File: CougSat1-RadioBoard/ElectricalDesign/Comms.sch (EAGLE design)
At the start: 409 parts, among them J1 700mm Antenna, J2 CougSat Card, J3 230mm Antenna, J4 SWD, Q1 DMN53D0LDW, Q2 DMN53D0LDW, Q3 DMN53D0LDW, Q4 CSD25402Q3A, Q5 CSD25402Q3A, U1 AD8515, U10 AD8515, U11 AD8515, U12 TXS0102DQM, U13 ADF4360, U14 MAAM-011229, U15 INA199C2, U16 AD8515, U17 AD8515, U18 LP5907MFX-3.1, U19 HMC545A, U2 AD8515, U20 INA199C1, U21 TPS61236, U22 AD8345, U23 AD9761, U24 TXS0102DQM, U25 TXS0102DQM, U26 TXS0102DQM, U27 MMZ09332B, U28 AD8515, U29 ADF4360, U3 AD7291, U30 TXS0102DQM, U31 INA199C2, U32 TXS0102DQM, U33 LP5907MFX-3.1, U34 MAAM-011229, U35 TXS0102DQM, U36 TXS0102DQM, U37 AD9761, U38 AD8346, U39 TXS0102DQM, U4 AD7291, U40 STM32L496VGT, U41 HMC452QS16G, U42 TXS0102DQM, U43 INA199C2, U44 ADF4360, U45 LP5907MFX-3.1, U46 IS25LP016D, U47 IS25LP016D, U48 GRF2133, U49 INA199C1, U5 MAAM-011229, U6 AD8348, U7 AD7291, U8 MAAM-011229, U9 TXS0102DQM, Y1 19.68MHz ±2.5ppm, Y2 19.68MHz ±2.5ppm, Y3 8MHz ±10ppm, Y4 32.768kHz ±10ppm, Y5 19.68MHz ±2.5ppm

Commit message: Removed 230mm circuits
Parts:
- removed C140, C143, C176: 1nF 1%, CougsInSpace-Capacitors:CAP-H-1NF-B-1608
- removed C141, C170, C172, C173, C174, C185: 1µF 10%, CougsInSpace-Capacitors:CAP-V-1UF-B-1608
- removed C142: 560pF 1%, CougsInSpace-Capacitors:CAP-V-560PF-1608
- removed C144: 100pF 1%, CougsInSpace-Capacitors:CAP-H-100PF-1608
- removed C145: 2pF ±0.1pF, CougsInSpace-Capacitors:CAP-V-2PF-1608
- removed C146, C147, C150, C156, C157, C158, C159, C160, C161, C163, C165, C166, C175, C178, C179, C180, C183, C184: 100nF 10%, CougsInSpace-Capacitors:CAP-V-100NF-1608
- removed C148, C171: 10nF 10%, CougsInSpace-Capacitors:CAP-V-10NF-1608
- removed C149, C168: 100pF 1%, CougsInSpace-Capacitors:CAP-V-100PF-1608
- removed C151, C155: 8pF ±0.25, CougsInSpace-Capacitors:CAP-V-8PF-1608
- removed C152: 56pF 2%, CougsInSpace-Capacitors:CAP-V-56PF-1608
- removed C153: 270pF 1%, CougsInSpace-Capacitors:CAP-V-270PF-1608
- removed C154: 10pF 5%, CougsInSpace-Capacitors:CAP-V-10PF-1608
- removed C162, C167: 15pF 1%, CougsInSpace-Capacitors:CAP-V-15PF-1608
- removed C164: 0.8pF ±0.1pF, CougsInSpace-Capacitors:CAP-H-0.8PF-1608
- removed C169: 4.7pF ±0.1, CougsInSpace-Capacitors:CAP-V-4.7PF-1608
- removed C177: 10pF 5%, CougsInSpace-Capacitors:CAP-H-10PF-1608
- removed C181, C182: 33pF 5%, CougsInSpace-Capacitors:CAP-H-33PF-1608
- removed FB8: 1.5kΩ @ 100MHz, CougsInSpace-Coils:CHOKE-V-1.5K-1608
- removed H5, H6, H7: M2, CougsInSpace-Hardware:MOUNTING_HOLE-2.2
- removed J4: SWD, CougsInSpace-Connectors:SWDSMD-6-R
- removed L13, L20: 22nH 2%, CougsInSpace-Coils:INDUCTOR-V-22NH-1608
- removed L14, L15, L16: 1.6nH 5%, CougsInSpace-Coils:INDUCTOR-V-1.6NH-1608
- removed L17: 22nH 2%, CougsInSpace-Coils:INDUCTOR-H-22NH-1608
- removed L18: 33nH 2%, CougsInSpace-Coils:INDUCTOR-V-33NH-1608
- removed L19: 18nH 2%, CougsInSpace-Coils:INDUCTOR-V-18NH-1608
- removed Q5: CSD25402Q3A, CougsInSpace-DiscreteSemi:MOSFET-P-SON-3333
- removed R75, R82, R89: 1kΩ 0.1%, CougsInSpace-Resistors:RES-V-1K-1608
- removed R76, R80: 49.9Ω 0.1%, CougsInSpace-Resistors:RES-V-49.9-1608
- removed R77, R79: 1.33kΩ 0.1%, CougsInSpace-Resistors:RES-V-1.33K-1608
- removed R78: 1.74kΩ 0.1%, CougsInSpace-Resistors:RES-V-1.74K-1608
- removed R81: 5.6Ω 1%, CougsInSpace-Resistors:RES-V-5.6R-1608
- removed R83: 102kΩ 0.1%, CougsInSpace-Resistors:RES-V-102K-1608
- removed R84: 0Ω <20mΩ, CougsInSpace-Resistors:RES-V-0-1608
- removed R85, R93: 50mΩ 1%, CougsInSpace-Resistors:RES-V-0.05R-1608
- removed R86, R92, R94, R95: 10kΩ 0.1%, CougsInSpace-Resistors:RES-V-10K-1608
- removed R87, R91: 4.7kΩ 0.1%, CougsInSpace-Resistors:RES-V-4.7K-1608
- removed R88: 75Ω 0.1%, CougsInSpace-Resistors:RES-V-75R-1608
- removed R90: 0Ω <20mΩ, CougsInSpace-Resistors:RES-H-0-1608
- removed U40: STM32L496VGT, CougsInSpace-IC-µController:STM32-100P-L496VGT
- removed U41: HMC452QS16G, CougsInSpace-RF:AMP-BIAS-HMC452QS16G
- removed U42: TXS0102DQM, CougsInSpace-IC-Comms:LEVEL_SHIFTER-2BIT-XSON-8
- removed U43: INA199C2, CougsInSpace-IC-Amplifiers:INA199C2
- removed U44: ADF4360, CougsInSpace-RF:ADF4360
- removed U45: LP5907MFX-3.1, CougsInSpace-IC-Power:LDO-3.1-SOT23-5
- removed U46, U47: IS25LP016D, CougsInSpace-IC-Memory:FLASH-(Q)SPI-2MB-SO8
- removed U48: GRF2133, CougsInSpace-RF:GRF2133
- removed U49: INA199C1, CougsInSpace-IC-Amplifiers:INA199C1
- removed Y5: 19.68MHz ±2.5ppm, CougsInSpace-Clocks:OSCILLATOR-19.68M-SMD-3225
- C112: value 100nF 10% -> 2.4pF ±0.1pF; device CougsInSpace-Capacitors:CAP-V-100NF-1608 -> CougsInSpace-Capacitors:CAP-H-2.4PF-1608
- C113: value 2.4pF ±0.1pF -> 100nF 10%; device CougsInSpace-Capacitors:CAP-H-2.4PF-1608 -> CougsInSpace-Capacitors:CAP-V-100NF-1608
- C114: value 100nF 10% -> 47pF 5%; device CougsInSpace-Capacitors:CAP-V-100NF-1608 -> CougsInSpace-Capacitors:CAP-V-47PF-1608
- C115: value 47pF 5% -> 100pF 1%; device CougsInSpace-Capacitors:CAP-V-47PF-1608 -> CougsInSpace-Capacitors:CAP-V-100PF-1608
- C116: value 100pF 1% -> 1µF 10%; device CougsInSpace-Capacitors:CAP-V-100PF-1608 -> CougsInSpace-Capacitors:CAP-V-1UF-B-1608
- C117: value 1µF 10% -> 1nF 1%; device CougsInSpace-Capacitors:CAP-V-1UF-B-1608 -> CougsInSpace-Capacitors:CAP-V-1NF-B-1608
- C118, C128: value 1nF 1% -> 100nF 10%; device CougsInSpace-Capacitors:CAP-V-1NF-B-1608 -> CougsInSpace-Capacitors:CAP-V-100NF-1608
- C119: value 100nF 10% -> 1µF 10%; device CougsInSpace-Capacitors:CAP-V-100NF-1608 -> CougsInSpace-Capacitors:CAP-V-1UF-B-1608
- C120: value 1µF 10% -> 1nF 1%; device CougsInSpace-Capacitors:CAP-V-1UF-B-1608 -> CougsInSpace-Capacitors:CAP-H-1NF-B-1608
- C121, C124: value 1nF 1% -> 1µF 10%; device CougsInSpace-Capacitors:CAP-H-1NF-B-1608 -> CougsInSpace-Capacitors:CAP-V-1UF-B-1608
- C122: value 1µF 10% -> 10nF 10%; device CougsInSpace-Capacitors:CAP-V-1UF-B-1608 -> CougsInSpace-Capacitors:CAP-V-10NF-1608
- C123: value 10nF 10% -> 1nF 1%; device CougsInSpace-Capacitors:CAP-V-10NF-1608 -> CougsInSpace-Capacitors:CAP-H-1NF-B-1608
- C125: value 1µF 10% -> 100nF 10%; device CougsInSpace-Capacitors:CAP-V-1UF-B-1608 -> CougsInSpace-Capacitors:CAP-V-100NF-1608
- C127: value 100nF 10% -> 1nF 1%; device CougsInSpace-Capacitors:CAP-V-100NF-1608 -> CougsInSpace-Capacitors:CAP-V-1NF-B-1608
- C130: value 560pF 1% -> 100nF 10%; device CougsInSpace-Capacitors:CAP-V-560PF-1608 -> CougsInSpace-Capacitors:CAP-V-100NF-1608
- C131: value 100nF 10% -> 8pF ±0.25; device CougsInSpace-Capacitors:CAP-V-100NF-1608 -> CougsInSpace-Capacitors:CAP-V-8PF-1608
- C132: value 100pF 1% -> 8pF ±0.25; device CougsInSpace-Capacitors:CAP-H-100PF-1608 -> CougsInSpace-Capacitors:CAP-V-8PF-1608
- C134, C136: value 100nF 10% -> 15pF 1%; device CougsInSpace-Capacitors:CAP-V-100NF-1608 -> CougsInSpace-Capacitors:CAP-V-15PF-1608
- C137: value 100pF 1% -> 100nF 10%; device CougsInSpace-Capacitors:CAP-V-100PF-1608 -> CougsInSpace-Capacitors:CAP-V-100NF-1608
- C138: value 10nF 10% -> 100nF 10%; device CougsInSpace-Capacitors:CAP-V-10NF-1608 -> CougsInSpace-Capacitors:CAP-V-100NF-1608
- C139: value 4.7pF ±0.1 -> 100nF 10%; device CougsInSpace-Capacitors:CAP-V-4.7PF-1608 -> CougsInSpace-Capacitors:CAP-V-100NF-1608
- H3: value Can - 230mm -> M2; device CougsInSpace-Hardware:SHIELDING-2641 -> CougsInSpace-Hardware:MOUNTING_HOLE-2.2
- J3: value 230mm Antenna -> SWD; device CougsInSpace-Connectors:COAX-U.FL -> CougsInSpace-Connectors:SWDSMD-6-R
- LOGO1: value SIGNATUREBRADLEY -> Satellite 16mm; device CougsInSpace-Aesthetics:SIGNATUREBRADLEY -> CougsInSpace-Aesthetics:CIS-LOGO-SATELLITE-16MM
- LOGO2: value Satellite 16mm -> SIGNATUREBRADLEY; device CougsInSpace-Aesthetics:CIS-LOGO-SATELLITE-16MM -> CougsInSpace-Aesthetics:SIGNATUREBRADLEY
- R61: value 0Ω <20mΩ -> 2kΩ 0.1%; device CougsInSpace-Resistors:RES-V-0-1608 -> CougsInSpace-Resistors:RES-V-2K-1608
- R62: value 2kΩ 0.1% -> 470Ω 0.5%; device CougsInSpace-Resistors:RES-V-2K-1608 -> CougsInSpace-Resistors:RES-V-470R-1608
- R63: value 470Ω 0.5% -> 1.74kΩ 0.1%; device CougsInSpace-Resistors:RES-V-470R-1608 -> CougsInSpace-Resistors:RES-V-1.74K-1608
- R64: value 1.74kΩ 0.1% -> 50mΩ 1%; device CougsInSpace-Resistors:RES-V-1.74K-1608 -> CougsInSpace-Resistors:RES-V-0.05R-1608
- R65: value 50mΩ 1% -> 10kΩ 0.1%; device CougsInSpace-Resistors:RES-V-0.05R-1608 -> CougsInSpace-Resistors:RES-V-10K-1608
- R66: value 10kΩ 0.1% -> 4.7kΩ 0.1%; device CougsInSpace-Resistors:RES-V-10K-1608 -> CougsInSpace-Resistors:RES-V-4.7K-1608
- R67: value 4.7kΩ 0.1% -> 2kΩ 0.1%; device CougsInSpace-Resistors:RES-V-4.7K-1608 -> CougsInSpace-Resistors:RES-V-2K-1608
- R69: value 2kΩ 0.1% -> 1kΩ 0.1%; device CougsInSpace-Resistors:RES-V-2K-1608 -> CougsInSpace-Resistors:RES-V-1K-1608
- R71: value 1.33kΩ 0.1% -> 1kΩ 0.1%; device CougsInSpace-Resistors:RES-V-1.33K-1608 -> CougsInSpace-Resistors:RES-V-1K-1608
- R72: value 1.74kΩ 0.1% -> 0Ω <20mΩ; device CougsInSpace-Resistors:RES-V-1.74K-1608 -> CougsInSpace-Resistors:RES-H-0-1608
- R73: value 1.33kΩ 0.1% -> 10kΩ 0.1%; device CougsInSpace-Resistors:RES-V-1.33K-1608 -> CougsInSpace-Resistors:RES-V-10K-1608
- R74: value 8.45kΩ 0.1% -> 10kΩ 0.1%; device CougsInSpace-Resistors:RES-V-8.45K-1608 -> CougsInSpace-Resistors:RES-V-10K-1608
- U37: value AD9761 -> STM32L496VGT; device CougsInSpace-IC-Conversion:AD9761 -> CougsInSpace-IC-µController:STM32-100P-L496VGT
- U38: value AD8346 -> IS25LP016D; device CougsInSpace-RF:AD834X6 -> CougsInSpace-IC-Memory:FLASH-(Q)SPI-2MB-SO8
- U39: value TXS0102DQM -> IS25LP016D; device CougsInSpace-IC-Comms:LEVEL_SHIFTER-2BIT-XSON-8 -> CougsInSpace-IC-Memory:FLASH-(Q)SPI-2MB-SO8
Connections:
- removed net !230_CS: U39.B1, U44.LE
- removed net !PC_5.0V-0: Q5.G, R92.1, U40D.PD5
- removed net !RFCLK_CS-230: U39.A1, U40B.PB3
- removed net 230_MOSI: U42.B2, U44.DATA
- removed net 230_SCK: U42.B1, U44.CLK
- removed net 3.1V_0: C131.1, C135.1, C137.1, C138.1, C148.1, C149.1, C156.1, C157.1, C161.1, C163.1, C170.1, C174.1, FB8.2, R76.2, R80.2, U37.AVDD, U38.ENBL, U38.VPS1, U38.VPS2, U39.OE, U39.VCCB, U42.OE, U42.VCCB, U44.AVDD, U44.CE, U44.DVDD, U44.VVCO, U45.OUT
- removed net 5.0V_0: C141.1, C144.1, C168.1, C172.1, C175.1, C185.1, L13.2, L18.2, R87.2, R88.2, R93.1, U41.VBIAS, U49.IN-
- removed net ANTENNA_230_COAX: C132.2, J3.CENTER
- removed net CHASSIS_230-0: C111.1, H5.MOUNT, R61.2
- removed net CHASSIS_230-1: C165.1, H4.MOUNT, R84.2
- removed net DAC_BUS_CLK-230: U37.CLOCK, U37.WRITE, U40E.PE5
- removed net DAC_COMP1-230: C129.1, U37.COMP1
- removed net DAC_COMP2-230: C135.2, U37.COMP2
- removed net DAC_COMP3-230: C146.1, U37.COMP3
- removed net DAC_FSADJ-230: R75.2, U37.FSADJ
- removed net DAC_FSASJ_MID-230: R74.2, R75.1
- removed net DAC_REFIO-230: C136.1, U37.REFIO
- removed net DAC_SLEEP-230: U37.SLEEP, U40D.PD7
- removed net I_3.1V-0: U4.IN4, U43.OUT
- removed net I_3.1V-0N: C173.1, R85.1, U43.IN-, U45.IN
- removed net I_5.0V-0: U4.IN3, U49.OUT
- removed net I_5.0V-0P: Q5.D, R93.2, U49.IN+
- removed net MOD_230_ID_N: C130.2, R72.1, R73.2, U37.IOUTN, U38.IBB_N
- removed net MOD_230_ID_P: C130.1, R71.2, R72.2, U37.IOUTP, U38.IBB_P
- removed net MOD_230_LOI_N: C140.2, U38.LOI_N
- removed net MOD_230_LOI_P: C143.2, U38.LOI_P
- removed net MOD_230_QD_N: C142.2, R77.2, R78.1, U37.QOUTN, U38.QBB_N
- removed net MOD_230_QD_P: C142.1, R78.2, R79.2, U37.QOUTP, U38.QBB_P
- removed net MOD_230_RFOUT: C154.1, C164.1, L14.2, U38.RFOUT
- removed net MOD_LNA_230_EN: R87.1, U48.VEN
- removed net MOD_LNA_230_RFIN: C181.2, U48.RFIN
- removed net MOD_LNA_230_RFINMID1: C164.2, L17.1
- removed net MOD_LNA_230_RFINMID2: C181.1, L17.2, L19.2
- removed net MOD_LNA_230_RFOUT: C182.1, L18.1, U48.RFOUT
- removed net MOD_LNA_230_VDD1: R88.1, U48.VDD1
- removed net MOD_PA_230_RC: C144.2, R81.2
- removed net MOD_PA_230_RFIN: C169.1, C177.2, U41.RFIN
- removed net MOD_PA_230_RFINMID: C177.1, C182.2, L20.2
- removed net MOD_PA_230_RFOUT: C132.1, C139.1, C145.1, L13.1, U41.RFOUT
- removed net MUXOUT-230: U40B.PB4, U44.MUXOUT
- removed net PC_3.1V-0: R86.2, U40D.PD6, U45.EN
- removed net REF_CLK_VDD-0: C178.1, FB8.1, Y5.VDD
- removed net RFCLK_CC-230: C171.1, U44.CC
- removed net RFCLK_CN-230: C174.2, U44.CN
- removed net RFCLK_CP-230: C152.1, R83.2, U44.CP, U44.VTUNE
- removed net RFCLK_L1-230: L15.2, U44.L1
- removed net RFCLK_L2-230: L16.2, U44.L2
- removed net RFCLK_OUT-230_N: C140.1, R76.1, U44.RFOUT_N
- removed net RFCLK_OUT-230_P: C143.1, R80.1, U44.RFOUT_P
- removed net RFCLK_REFIN-230: C176.2, U44.REFIN
- removed net RFCLK_REFOUT-230: C176.1, Y5.OUT
- removed net RFCLK_RSET-230: R91.2, U44.RSET
- removed net RFCLK_VTUNE_FILTER-230: C153.1, R83.1
- removed net TEMP_CLK_230: RN3.7, RT15.1, U7.IN4
- removed net TEMP_DAC_230: RN3.6, RT12.1, U7.IN2
- removed net TEMP_LDO-0: RN3.3, RT16.1, U7.IN3
- removed net TEMP_MOD_230: RN3.8, RT13.1, U7.IN6
- removed net TEMP_PA_230: RN3.2, RT14.1, U7.IN5
- new net TEMP_PCB_0: RN3.6, RT13.1, U7.IN2
- new net TEMP_PCB_1: RN3.3, RT15.1, U7.IN3
- new net TEMP_PCB_2: RN3.7, RT14.1, U7.IN4
- new net TEMP_PCB_3: RN3.2, RT16.1, U7.IN5
- new net TEMP_PCB_4: RN3.8, RT11.1, U7.IN6
- net !ADC_RESET: now also U37A.PA4; no longer U40A.PA4
- net !COM_SPI_CS: now also U37B.PB0; no longer U40B.PB0
- net !FLASH_CS-A: now also U37B.PB5, U39.!CE; no longer U40B.PB5, U47.!CE
- net !FLASH_CS-B: now also U37B.PB8, U38.!CE; no longer U40B.PB8, U46.!CE
- net !FLASH_WP: now also U37B.PB9, U38.!WP!(IO2), U39.!WP!(IO2); no longer U40B.PB9, U46.!WP!(IO2), U47.!WP!(IO2)
- net !NRST: now also C130.1, J3.!RST, U37BASE.!NRST; no longer C147.1, J4.!RST, U40BASE.!NRST
- net !PC_5.0V-1: now also U37C.PC2; no longer U40C.PC2
- net !RFCLK_CS-DEMOD: now also U37C.PC3; no longer U40C.PC3
- net !RFCLK_CS-MOD: now also U37D.PD2; no longer U40D.PD2
- net !RX_LNA_EN: now also U37C.PC0; no longer U40C.PC0
- net 3.1V_1: now also C111.1, C113.1, C117.1, C119.1, C121.1, R67.2; no longer C112.1, C115.1, C118.1, C120.1, C122.1, R68.2
- net 3.3V_5: now also C118.1; no longer C119.1
- net 3.3V_6: now also C126.1, C128.1, C129.1, C135.1, C137.1, C138.1, C139.1, R64.2, R71.2, R73.2, R74.2, U37BASE.VBAT, U37BASE.VDD@1, U37BASE.VDD@2, U37BASE.VDD@3, U37BASE.VDD@4, U37BASE.VDD@5, U37BASE.VDDUSB, U38.VCC, U39.VCC; no longer C127.1, C134.1, C150.1, C159.1, C160.1, C166.1, C179.1, C183.1, C184.1, R65.2, R85.2, R89.2, R94.2, R95.2, U37.DVDD, U39.VCCA, U40BASE.VBAT, U40BASE.VDD@1, U40BASE.VDD@2, U40BASE.VDD@3, U40BASE.VDD@4, U40BASE.VDD@5, U40BASE.VDDUSB, U42.VCCA, U43.IN+, U46.VCC, U47.VCC
- net 5.0V: no longer Q5.S, R92.2
- net 5.0V_1: now also C115.1, R61.2, R63.2; no longer C117.1, R62.2, R64.2
- net AGND: now also U37BASE.VREF-, U37BASE.VSSA; no longer C158.2, C180.2, U40BASE.VREF-, U40BASE.VSSA, U43.GND, U43.REF, U49.GND, U49.REF
- net ANTENNA_SW: now also U37D.PD1; no longer U40D.PD1
- net AVDD: now also U37BASE.VDDA, U37BASE.VREF+; no longer C158.1, C180.1, U40BASE.VDDA, U40BASE.VREF+, U43.VDD, U49.VDD
- net BOOT0: now also R72.2, U37BASE.BOOT0; no longer R90.2, U40BASE.BOOT0
- net CHASSIS_700-0: now also H4.MOUNT; no longer H7.MOUNT
- net CHASSIS_700-1: now also H3.MOUNT; no longer H6.MOUNT
- net COM_SPI_MISO: now also U37A.PA6; no longer U40A.PA6
- net COM_SPI_MOSI: now also U37A.PA7; no longer U40A.PA7
- net COM_SPI_SCK: now also U37A.PA0; no longer U40A.PA0
- net CTRL_SYNC: now also U37C.PC4; no longer U40C.PC4
- net DAC_BUS_0: now also U37E.PE6; no longer U37.DB0(LSB), U40E.PE6
- net DAC_BUS_1: now also U37E.PE7; no longer U37.DB1, U40E.PE7
- net DAC_BUS_2: now also U37E.PE8; no longer U37.DB2, U40E.PE8
- net DAC_BUS_3: now also U37E.PE9; no longer U37.DB3, U40E.PE9
- net DAC_BUS_4: now also U37E.PE10; no longer U37.DB4, U40E.PE10
- net DAC_BUS_5: now also U37E.PE11; no longer U37.DB5, U40E.PE11
- net DAC_BUS_6: now also U37E.PE12; no longer U37.DB6, U40E.PE12
- net DAC_BUS_7: now also U37E.PE13; no longer U37.DB7, U40E.PE13
- net DAC_BUS_8: now also U37E.PE14; no longer U37.DB8, U40E.PE14
- net DAC_BUS_9: now also U37E.PE15; no longer U37.DB9(MSB), U40E.PE15
- net DAC_BUS_CLK-700: now also U37E.PE4; no longer U40E.PE4
- net DAC_SELECT_I/!Q: now also U37E.PE3; no longer U37.SELECT-I/!Q, U40E.PE3
- net DAC_SLEEP-700: now also U37C.PC5; no longer U40C.PC5
- net DEMOD_ENABLE: now also U37A.PA2; no longer U40A.PA2
- net DEMOD_ID: now also U37A.PA1; no longer U40A.PA1
- net DEMOD_QD: now also U37A.PA3; no longer U40A.PA3
- net DEMOD_VGIN: now also U37A.PA5; no longer U40A.PA5
- net DGND: now also C113.2, C121.2, C124.2, C130.2, C132.2, C135.2, J3.DGND, R62.1, R65.1, R68.1, R72.1, U37BASE.VSS@1, U37BASE.VSS@2, U37BASE.VSS@3, U37BASE.VSS@4, U37BASE.VSS@5; no longer C112.2, C119.2, C123.2, C141.2, C145.2, C146.2, C147.2, C148.2, C149.2, C150.2, C151.2, C152.2, C153.2, C154.2, C155.2, C156.2, C157.2, C159.2, C160.2, C161.2, C162.2, C163.2, C165.2, C166.2, C167.2, C168.2, C169.2, C170.2, C171.2, C172.2, C173.2, C175.2, C178.2, C179.2, C183.2, C184.2, C185.2, H3.SHIELD, J3.SHIELD, J4.DGND, L14.1, L15.1, L16.1, L19.1, L20.1, R61.1, R63.1, R67.1, R71.1, R73.1, R74.1, R77.1, R79.1, R81.1, R82.1, R84.1, R86.1, R90.1, R91.1, U37.AVSS, U37.DVSS, U37.REFLO, U38.RFGND, U39.A2, U39.B2, U40BASE.VSS@1, U40BASE.VSS@2, U40BASE.VSS@3, U40BASE.VSS@4, U40BASE.VSS@5, U41.RFGND, U42.DGND, U44.AGND, U44.CPGND, U44.DGND, U44.PAD, U45.PGND, U46.DGND, U47.DGND, U48.RFGND, Y5.GND
- net FLASH_HOLD-A: now also R73.1, U39.!HOLD!(IO3); no longer R94.1, U47.!HOLD!(IO3)
- net FLASH_HOLD-B: now also R74.1, U38.!HOLD!(IO3); no longer R95.1, U46.!HOLD!(IO3)
- net I2C_SCL: now also U37B.PB6; no longer U40B.PB6
- net I2C_SDA: now also U37B.PB7; no longer U40B.PB7
- net I_3.1V-1N: now also C124.1, R64.1; no longer C125.1, R65.1
- net JTAG_EN_COMMS: now also R69.2; no longer R70.2
- net JTAG_TCK: now also J3.SWCLK, U37A.PA14; no longer J4.SWCLK, U40A.PA14
- net JTAG_TDI: now also U37A.PA15; no longer U40A.PA15
- net JTAG_TDO: now also J3.SWO, U37B.PB2; no longer J4.SWO, U40B.PB2
- net JTAG_TMS: now also J3.SWDIO, U37A.PA13; no longer J4.SWDIO, U40A.PA13
- net LED_A: now also U37D.PD8; no longer U40D.PD8
- net LED_C: now also R70.2; no longer R82.2
- net MOD_700_RFOUT: now also C112.1; no longer C113.1
- net MOD_LNA_700_RFINMID: now also C112.2; no longer C113.2
- net MOD_LNA_700_RFOUT: now also C123.1; no longer C124.1
- net MOD_PA_700_RFINMID: now also C123.2; no longer C124.2
- net MUXOUT-DEMOD: now also U37D.PD0; no longer U40D.PD0
- net MUXOUT-MOD: now also U37D.PD4; no longer U40D.PD4
- net OSC32_IN: now also C136.1, U37C.PC14; no longer C167.1, U40C.PC14
- net OSC32_OUT: now also C134.1, U37C.PC15; no longer C162.1, U40C.PC15
- net OSC_IN: now also C132.1, U37BASE.PH0-OSC_IN; no longer C155.1, U40BASE.PH0-OSC_IN
- net OSC_OUT: now also C131.1, U37BASE.PH1-OSC_OUT; no longer C151.1, U40BASE.PH1-OSC_OUT
- net PA_PD-700: now also U37D.PD3; no longer U40D.PD3
- net PA_VBA1-700: now also R63.1; no longer R64.1
- net PA_VBA2-700: now also R61.1; no longer R62.1
- net PC_3.1V-1: now also R65.2, U37C.PC13; no longer R66.2, U40C.PC13
- net PC_3.1V-2: now also U37C.PC1; no longer U40C.PC1
- net PREAMP_700_BIAS: now also C127.1, R67.1, R68.2; no longer C128.1, R68.1, R69.2
- net REF_CLK_VDD-1: now also C125.1; no longer C126.1
- net REG_EN-5: now also U37B.PB10; no longer U40B.PB10
- net RFCLK_CC-MOD: now also C122.1; no longer C123.1
- net RFCLK_CN-MOD: now also C119.2; no longer C120.2
- net RFCLK_L2-MOD: now also R62.2; no longer R63.2
- net RFCLK_REFIN-MOD: now also C120.2; no longer C121.2
- net RFCLK_REFOUT-MOD: now also C120.1; no longer C121.1
- net RFCLK_RSET-MOD: now also R66.2; no longer R67.2
- net SPI_MISO: now also U37C.PC11, U38.SO(IO1), U39.SO(IO1); no longer U40C.PC11, U46.SO(IO1), U47.SO(IO1)
- net SPI_MOSI: now also U37C.PC12, U38.SI(IO0), U39.SI(IO0); no longer U40C.PC12, U42.A2, U46.SI(IO0), U47.SI(IO0)
- net SPI_SCK: now also U37C.PC10, U38.CLK, U39.CLK; no longer U40C.PC10, U42.A1, U46.CLK, U47.CLK
- net SWD_VSENSE: now also J3.VSENSE, R71.1; no longer J4.VSENSE, R89.1
- net TEMP_COMMS: now also RT12.1; no longer RT11.1
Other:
- note added: "Page 10"
- note added: "Page 10: Baseband & Carrier - 700 Page 11: 700mm Downlink Page 12: 700mm Uplink Amplifiers Page 13: Demodulator Page 14: Mechanical"
- note added: "Page 1: Block Diagram Page 2: RF Diagram Page 3: Power Rails Page 4: µController Page 5: Buffers Page 6: ADCs Page 7: Regulator Page 8: Power Switching & LDOs Page 9: Baseband & Carrier - 700"
- note added: "Pages 11"
- note removed: "12A1>"
- note removed: "12A2>"
- note removed: "20mA + 45mA"
- note removed: "230mm"
- note removed: "230mm TX"
- note removed: "3.1V-0"
- note removed: "3080mW"
- note removed: "490mA"
- note removed: "5.0V-0"
- note removed: "60mA"
- note removed: "8A2>"
- note removed: "8A5>"
- note removed: "9A5>"
- note removed: "9B1>"
- note removed: "9C2>"
- note removed: "9C6>"
- note removed: "<9B3"
- note removed: "A"
- note removed: "B"
- note removed: "C"
- note removed: "CAD Note: Transmission Line"
- note removed: "Connector: To High Gain 230mm Antenna"
- note removed: "DAC Output: 0-2mA Converted: 1.2±0.5V -3dB at 280kHz"
- note removed: "Length 2mm Length 2.6mm Length 3mm"
- note removed: "Note: -8dBm"
- note removed: "Note: 21dBm"
- note removed: "Page 10: Baseband & Carrier - 700 Page 11: Baseband & Carrier - 700 Page 12: 230mm Downlink Page 13: 700mm Downlink Page 14: 700mm Uplink Amplifiers Page 15: Demodulator Page 16: Mechanical"
- note removed: "Page 11"
- note removed: "Page 1: Block Diagram Page 2: RF Diagram Page 3: Power Rails Page 4: µController Page 5: Buffers Page 6: ADCs Page 7: Regulator Page 8: Power Switching & LDOs Page 9: Baseband & Carrier - 230"
- note removed: "Pages 10"
- note removed: "Pages 10/11"
- note removed: "Pages 14"
- note removed: "Pages 15"

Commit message: Updated off-sheet connectors
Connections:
- net DAC_BUS_CLK-700 renamed DAC_BUS_CLK
- net PA_PD-700 renamed PA_PD
- net DGND: now also U4.IN3, U4.IN4
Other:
- note added: "10B3> 10C3>"
- note added: "10C1>"
- note added: "10D1>"
- note added: "11A1>"
- note added: "11A2>"
- note added: "11B2>"
- note added: "11C3>"
- note added: "11D2>"
- note added: "11D5>"
- note added: "12B1> 12B3> 12C2>"
- note added: "12C5>"
- note added: "12D3>"
- note added: "13A4>"
- note added: "13B1>"
- note added: "13B3>"
- note added: "13B4>"
- note added: "4A4> 9A1> 10A1>"
- note added: "6C5>"
- note added: "6D5>"
- note added: "9A5>"
- note added: "9B1>"
- note added: "9B2>"
- note added: "9C2>"
- note added: "9C6>"
- note added: "<10C3"
- note added: "<10C5"
- note added: "<10D3"
- note added: "<12B1"
- note added: "<9B3"
- note removed: "10A5>"
- note removed: "10C2>"
- note removed: "10C6>"
- note removed: "10D3>"
- note removed: "11A3>"
- note removed: "11A5>"
- note removed: "11B1>"
- note removed: "11B3> 11C3>"
- note removed: "11D1>"
- note removed: "12B2>"
- note removed: "12C3>"
- note removed: "13A2>"
- note removed: "13C1>"
- note removed: "13C3>"
- note removed: "13D2>"
- note removed: "13D5>"
- note removed: "14B1> 14B3> 14C2>"
- note removed: "14C5>"
- note removed: "14D3>"
- note removed: "15A1>"
- note removed: "15A4>"
- note removed: "15B1>"
- note removed: "15B2>"
- note removed: "15B3>"
- note removed: "15B4>"
- note removed: "230mm Downlink"
- note removed: "4A4> 9A1> 10A1> 11A1>"
- note removed: "8A3>"
- note removed: "9B2> 10B2>"
- note removed: "<11B3"
- note removed: "<11C3"
- note removed: "<11C5"
- note removed: "<11D3"
- note removed: "<14B1"

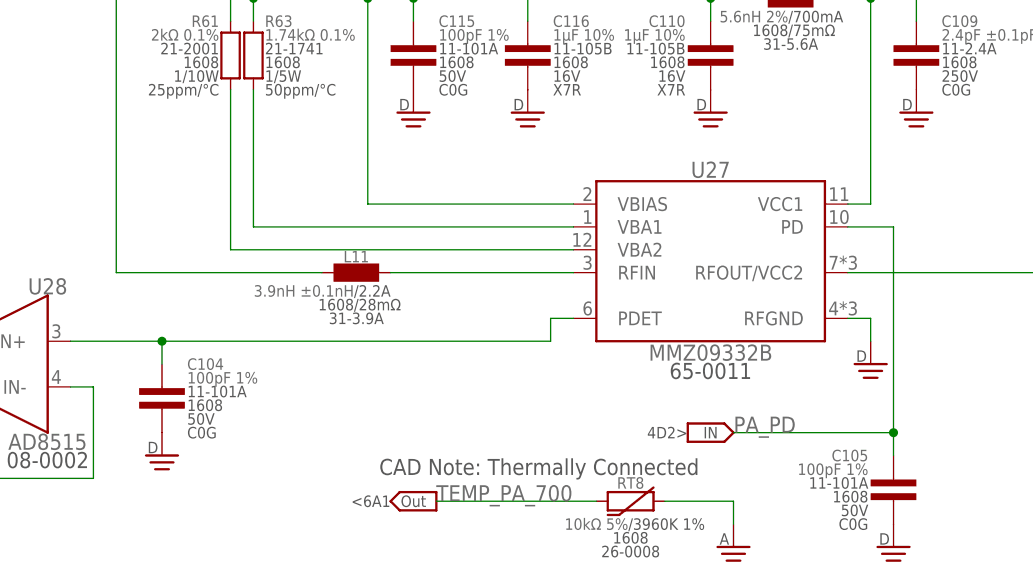
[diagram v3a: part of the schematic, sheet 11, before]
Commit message: added heatsink traces
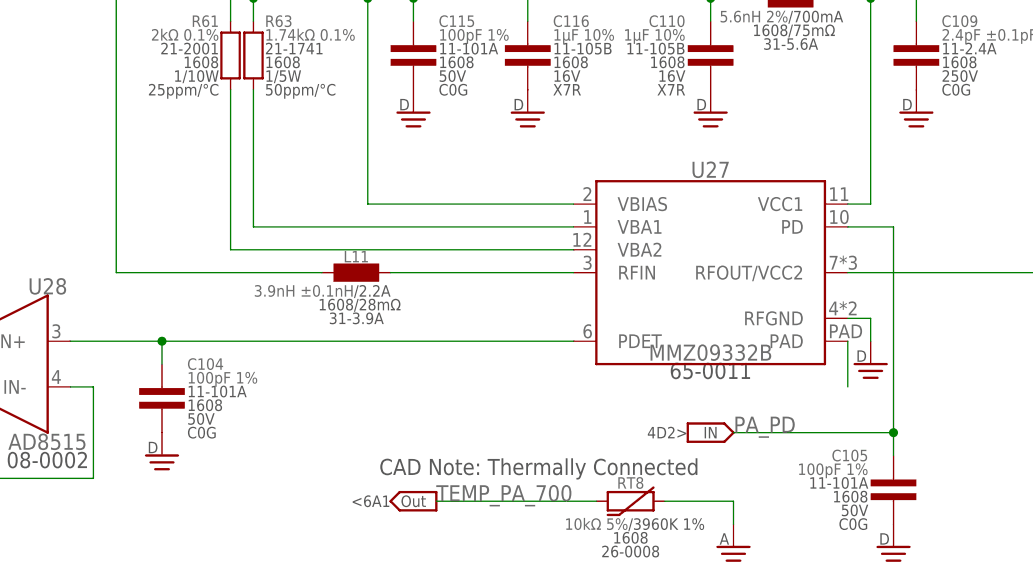
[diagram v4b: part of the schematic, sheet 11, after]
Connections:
- new net SELFNET: U27.PAD
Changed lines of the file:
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@@
 <pinref part="U27" gate="G$1" pin="PDET"/>
 <pinref part="U28" gate="G$1" pin="IN+"/>
-<wire x1="106.68" y1="73.66" x2="63.5" y2="73.66" width="0.1524" layer="91"/>
+<wire x1="109.22" y1="73.66" x2="63.5" y2="73.66" width="0.1524" layer="91"/>
 <pinref part="C104" gate="G$1" pin="1"/>
 <wire x1="63.5" y1="73.66" x2="53.34" y2="73.66" width="0.1524" layer="91"/>
 <wire x1="63.5" y1="71.12" x2="63.5" y2="73.66" width="0.1524" layer="91"/>
 <junction x="63.5" y="73.66"/>
-<wire x1="109.22" y1="76.2" x2="106.68" y2="76.2" width="0.1524" layer="91"/>
-<wire x1="106.68" y1="76.2" x2="106.68" y2="73.66" width="0.1524" layer="91"/>
 </segment>
 </net>
@@
 </segment>
 </net>
+<net name="SELFNET" class="0">
+<segment>
+<pinref part="U27" gate="G$1" pin="PAD"/>
+<wire x1="139.7" y1="73.66" x2="139.7" y2="68.58" width="0.1524" layer="91"/>
+</segment>
+</net>

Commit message: Adjusted layout
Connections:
- net SELFNET renamed PA_HEATSINK
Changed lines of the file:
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@@
 <instance part="U27" gate="G$1" x="124.46" y="81.28" smashed="yes">
 <attribute name="NAME" x="124.46" y="92.71" size="1.778" layer="95" align="center"/>
-<attribute name="VALUE" x="124.46" y="72.39" size="1.778" layer="96" align="center"/>
-<attribute name="SKU" x="124.46" y="70.358" size="1.778" layer="97" align="center"/>
+<attribute name="VALUE" x="124.46" y="69.85" size="1.778" layer="96" align="center"/>
+<attribute name="SKU" x="124.46" y="67.818" size="1.778" layer="97" align="center"/>
 </instance>
 <instance part="C76" gate="G$1" x="195.58" y="68.58" smashed="yes" rot="MR0">
@@
 </segment>
 </net>
-<net name="SELFNET" class="0">
+<net name="PA_HEATSINK" class="0">
 <segment>
 <pinref part="U27" gate="G$1" pin="PAD"/>

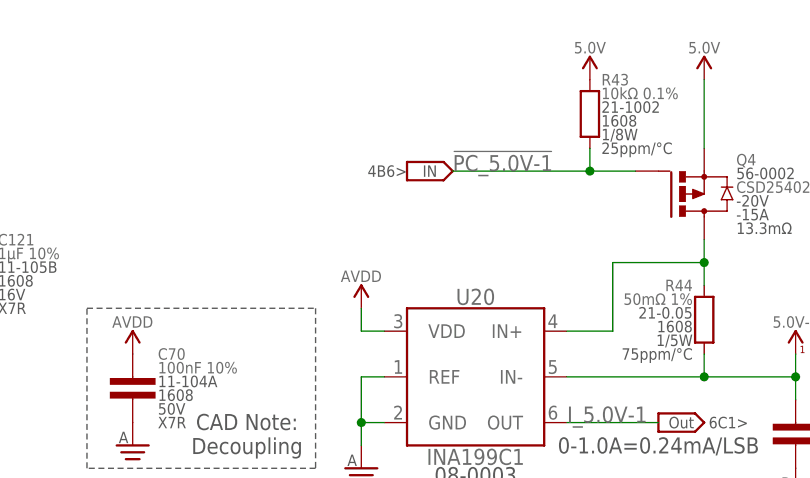
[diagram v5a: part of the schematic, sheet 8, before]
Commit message: Added nFET
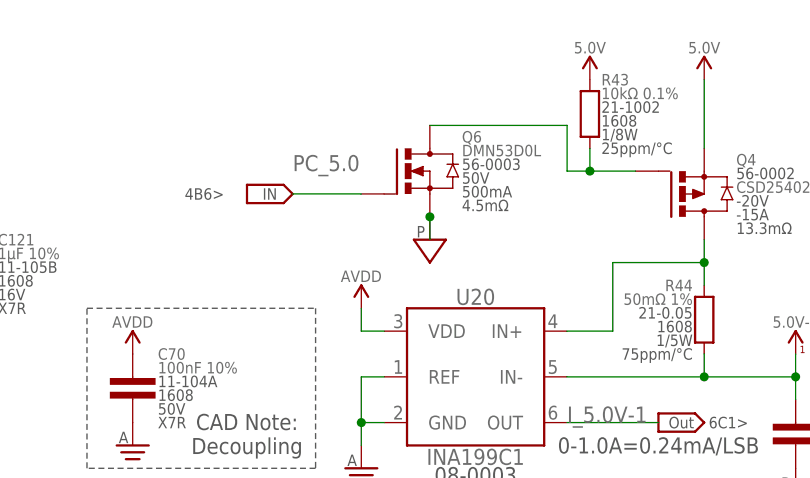
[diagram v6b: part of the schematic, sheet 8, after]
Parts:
- added Q6: DMN53D0L, CougsInSpace-DiscreteSemi:MOSFET-N-SOT23-3
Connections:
- new net PC_5.0: Q6.G
- net !PC_5.0V-1: now also Q6.D
- net PGND: now also Q6.S
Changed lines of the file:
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@@
 <parts>
 <part name="FRAME1" library="CougsInSpace-Aesthetics" deviceset="FRAME-A" device="">
+<attribute name="REV" value="1.3.0"/>
 <attribute name="TITLE" value="Block Diagram"/>
 </part>
@@
 <part name="OFFSHEET62" library="CougsInSpace-Aesthetics" deviceset="OFF_SHEET-OUT" device=""/>
 <part name="OFFSHEET158" library="CougsInSpace-Aesthetics" deviceset="OFF_SHEET-OUT" device=""/>
+<part name="SUPPLY5" library="CougsInSpace-PowerSymbols" deviceset="PGND" device=""/>
+<part name="Q6" library="CougsInSpace-DiscreteSemi" deviceset="MOSFET-N" device="-SOT23-3" value="DMN53D0L"/>
 </parts>
 <sheets>
@@
 <text x="96.52" y="121.92" size="1.27" layer="97" align="center-right">&lt;6A4 </text>
 <text x="96.52" y="58.42" size="1.27" layer="97" align="center-right">&lt;6A1 </text>
-<text x="182.88" y="111.76" size="1.27" layer="97" align="center-right">4B6&gt; </text>
+<text x="162.56" y="109.22" size="1.27" layer="97" align="center-right">4B6&gt; </text>
 <text x="71.12" y="30.48" size="1.27" layer="97" align="center-right">4B6&gt; </text>
 <text x="71.12" y="93.98" size="1.27" layer="97" align="center-right">4C6&gt; </text>
@@
 </instance>
 <instance part="SUPPLY427" gate="G$1" x="177.8" y="78.74" smashed="yes"/>
-<instance part="OFFSHEET74" gate="G$1" x="185.42" y="111.76" smashed="yes"/>
+<instance part="OFFSHEET74" gate="G$1" x="167.64" y="109.22" smashed="yes"/>
 <instance part="R43" gate="G$1" x="203.2" y="116.84" smashed="yes">
 <attribute name="NAME" x="204.47" y="121.92" size="1.27" layer="95" align="center-left"/>
@@
 <instance part="SUPPLY331" gate="1" x="96.52" y="17.78" smashed="yes"/>
 <instance part="SUPPLY332" gate="1" x="91.44" y="17.78" smashed="yes"/>
+<instance part="SUPPLY5" gate="G$1" x="185.42" y="104.14" smashed="yes"/>
+<instance part="Q6" gate="G$1" x="185.42" y="111.76" smashed="yes">
+<attribute name="NAME" x="188.976" y="115.57" size="1.27" layer="95" align="center-left"/>
+<attribute name="VALUE" x="188.976" y="114.046" size="1.27" layer="96" align="center-left"/>
+<attribute name="SKU" x="188.976" y="112.522" size="1.27" layer="97" align="center-left"/>
+<attribute name="VDS" x="188.976" y="110.998" size="1.27" layer="97" align="center-left"/>
+<attribute name="CURRENT" x="188.976" y="109.474" size="1.27" layer="97" align="center-left"/>
+<attribute name="RDS" x="188.976" y="107.95" size="1.27" layer="97" align="center-left"/>
+</instance>
 </instances>
 <busses>
@@
 <pinref part="Q4" gate="G$1" pin="G"/>
 <wire x1="208.28" y1="111.76" x2="203.2" y2="111.76" width="0.1524" layer="91"/>
-<label x="187.96" y="111.76" size="1.778" layer="97"/>
 <pinref part="R43" gate="G$1" pin="1"/>
-<wire x1="203.2" y1="111.76" x2="187.96" y2="111.76" width="0.1524" layer="91"/>
 <wire x1="203.2" y1="114.3" x2="203.2" y2="111.76" width="0.1524" layer="91"/>
+<wire x1="185.42" y1="116.84" x2="200.66" y2="116.84" width="0.1524" layer="91"/>
+<wire x1="200.66" y1="116.84" x2="200.66" y2="111.76" width="0.1524" layer="91"/>
+<wire x1="200.66" y1="111.76" x2="203.2" y2="111.76" width="0.1524" layer="91"/>
 <junction x="203.2" y="111.76"/>
+<pinref part="Q6" gate="G$1" pin="D"/>
 </segment>
 </net>
@@
 </segment>
 </net>
+<net name="PC_5.0" class="0">
+<segment>
+<label x="170.18" y="111.76" size="1.778" layer="97"/>
+<wire x1="170.18" y1="109.22" x2="177.8" y2="109.22" width="0.1524" layer="91"/>
+<pinref part="Q6" gate="G$1" pin="G"/>
+</segment>
+</net>
+<net name="PGND" class="3">
+<segment>
+<wire x1="185.42" y1="106.68" x2="185.42" y2="104.14" width="0.1524" layer="91"/>
+<pinref part="SUPPLY5" gate="G$1" pin="PGND"/>
+<pinref part="Q6" gate="G$1" pin="S"/>
+<junction x="185.42" y="106.68"/>
+</segment>
+</net>

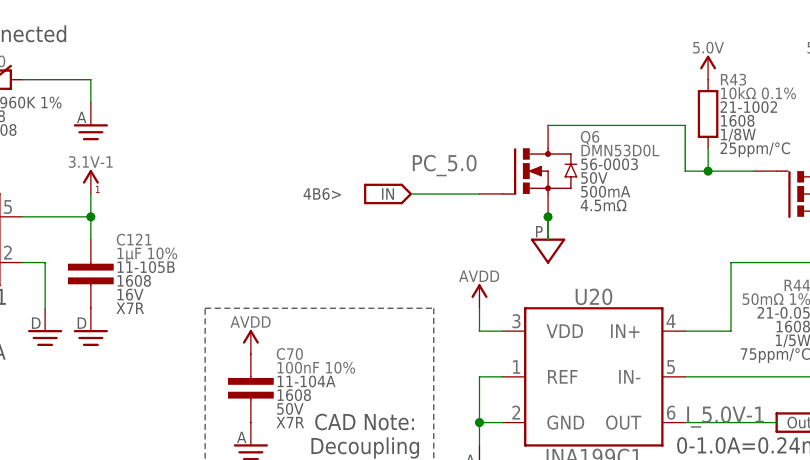
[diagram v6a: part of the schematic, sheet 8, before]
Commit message: Fixed net names
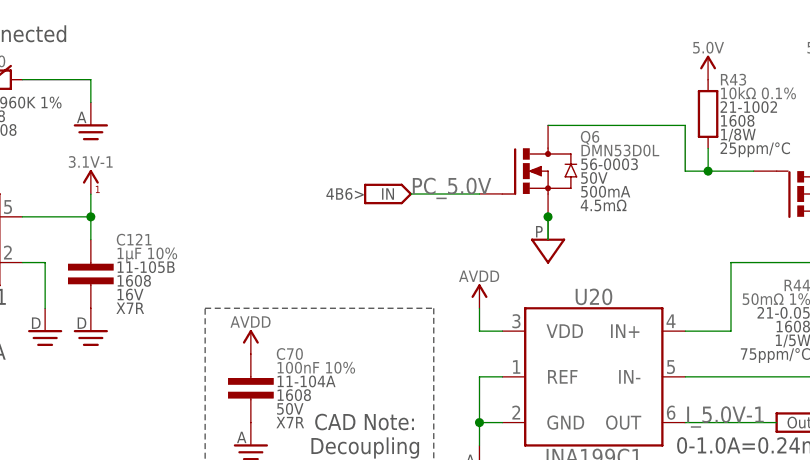
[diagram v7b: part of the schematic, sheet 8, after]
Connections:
- removed net !PC_5.0V-1: Q4.G, Q6.D, R43.1, U37C.PC2
- removed net PC_5.0: Q6.G
- new net !PC_5.0V: Q4.G, Q6.D, R43.1
- new net PC_5.0V: Q6.G, U37C.PC2
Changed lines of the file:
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@@
 </segment>
 </net>
-<net name="!PC_5.0V-1" class="0">
+<net name="!RX_LNA_EN" class="0">
+<segment>
+<wire x1="203.2" y1="104.14" x2="231.14" y2="104.14" width="0.1524" layer="91"/>
+<label x="204.47" y="104.14" size="1.778" layer="95"/>
+<pinref part="U37" gate="C" pin="PC0"/>
+</segment>
+</net>
+<net name="PC_5.0V" class="0">
 <segment>
 <wire x1="203.2" y1="99.06" x2="231.14" y2="99.06" width="0.1524" layer="91"/>
 <label x="204.47" y="99.06" size="1.778" layer="95"/>
 <pinref part="U37" gate="C" pin="PC2"/>
-</segment>
-</net>
-<net name="!RX_LNA_EN" class="0">
-<segment>
-<wire x1="203.2" y1="104.14" x2="231.14" y2="104.14" width="0.1524" layer="91"/>
-<label x="204.47" y="104.14" size="1.778" layer="95"/>
-<pinref part="U37" gate="C" pin="PC0"/>
 </segment>
 </net>
@@
 <text x="96.52" y="121.92" size="1.27" layer="97" align="center-right">&lt;6A4 </text>
 <text x="96.52" y="58.42" size="1.27" layer="97" align="center-right">&lt;6A1 </text>
-<text x="162.56" y="109.22" size="1.27" layer="97" align="center-right">4B6&gt; </text>
+<text x="165.1" y="109.22" size="1.27" layer="97" align="center-right">4B6&gt; </text>
 <text x="71.12" y="30.48" size="1.27" layer="97" align="center-right">4B6&gt; </text>
 <text x="71.12" y="93.98" size="1.27" layer="97" align="center-right">4C6&gt; </text>
@@
 </segment>
 </net>
-<net name="!PC_5.0V-1" class="0">
+<net name="!PC_5.0V" class="0">
 <segment>
 <pinref part="Q4" gate="G$1" pin="G"/>
@@
 </segment>
 </net>
-<net name="PC_5.0" class="0">
-<segment>
-<label x="170.18" y="111.76" size="1.778" layer="97"/>
+<net name="PC_5.0V" class="0">
+<segment>
+<label x="170.18" y="109.22" size="1.778" layer="97"/>
 <wire x1="170.18" y1="109.22" x2="177.8" y2="109.22" width="0.1524" layer="91"/>
 <pinref part="Q6" gate="G$1" pin="G"/>

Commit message: added new gerbers
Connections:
- net JTAG_TDO: now also U37B.PB3; no longer U37B.PB2
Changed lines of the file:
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@@
 <part name="DIA15" library="CougsInSpace-Aesthetics" deviceset="DIAGRAM-MEASURE-T" device=""/>
 <part name="FRAME2" library="CougsInSpace-Aesthetics" deviceset="FRAME-A" device="">
+<attribute name="REV" value="1.3.0"/>
 <attribute name="TITLE" value="RF Diagram"/>
 </part>
@@
 </segment>
 <segment>
-<wire x1="96.52" y1="93.98" x2="124.46" y2="93.98" width="0.1524" layer="91"/>
 <label x="97.79" y="93.98" size="1.778" layer="95"/>
-<pinref part="U37" gate="B" pin="PB2"/>
+<pinref part="U37" gate="B" pin="PB3"/>
+<wire x1="99.06" y1="93.98" x2="124.46" y2="93.98" width="0.1524" layer="91"/>
+<wire x1="96.52" y1="91.44" x2="99.06" y2="91.44" width="0.1524" layer="91"/>
+<wire x1="99.06" y1="91.44" x2="99.06" y2="93.98" width="0.1524" layer="91"/>
 </segment>
 </net>
